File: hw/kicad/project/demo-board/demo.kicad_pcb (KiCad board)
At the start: 2 copper layers, 49.5 x 49.5 mm, 20 parts, among them P1 CONN_01X16, P2 CONN_01X16, SW1 KEY_FLASH, SW2 KEY_RST, U1 NCP1117ST33T3G, U2 ESP-12E

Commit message: Freeroute applied
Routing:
- net /SPI_INT: track 0.00 -> 46.5 mm
- net /TXD0: track 0.00 -> 46.1 mm
- net /RXD0: track 0.00 -> 45.7 mm
- net /GPIO10: track 0.00 -> 43.4 mm, vias 0 -> 1
- net /GPIO0: track 0.00 -> 40.2 mm, vias 0 -> 1
- net /nRST: track 42.1 -> 80.1 mm
- net Net-(JP1-Pad2): track 0.00 -> 33.5 mm
- net /GPIO13: track 0.00 -> 32.3 mm
- net /GPIO12: track 0.00 -> 32.1 mm
- net /GPIO14: track 0.00 -> 31.9 mm
- net /EN: track 12.6 -> 42.5 mm
- net /GPIO16: track 10.2 -> 38.9 mm
- net VCC: track 60.6 -> 89.0 mm, vias 2 -> 3
- net /SPI_CLK: track 0.00 -> 28.2 mm
- net /GPIO9: track 0.00 -> 26.7 mm
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
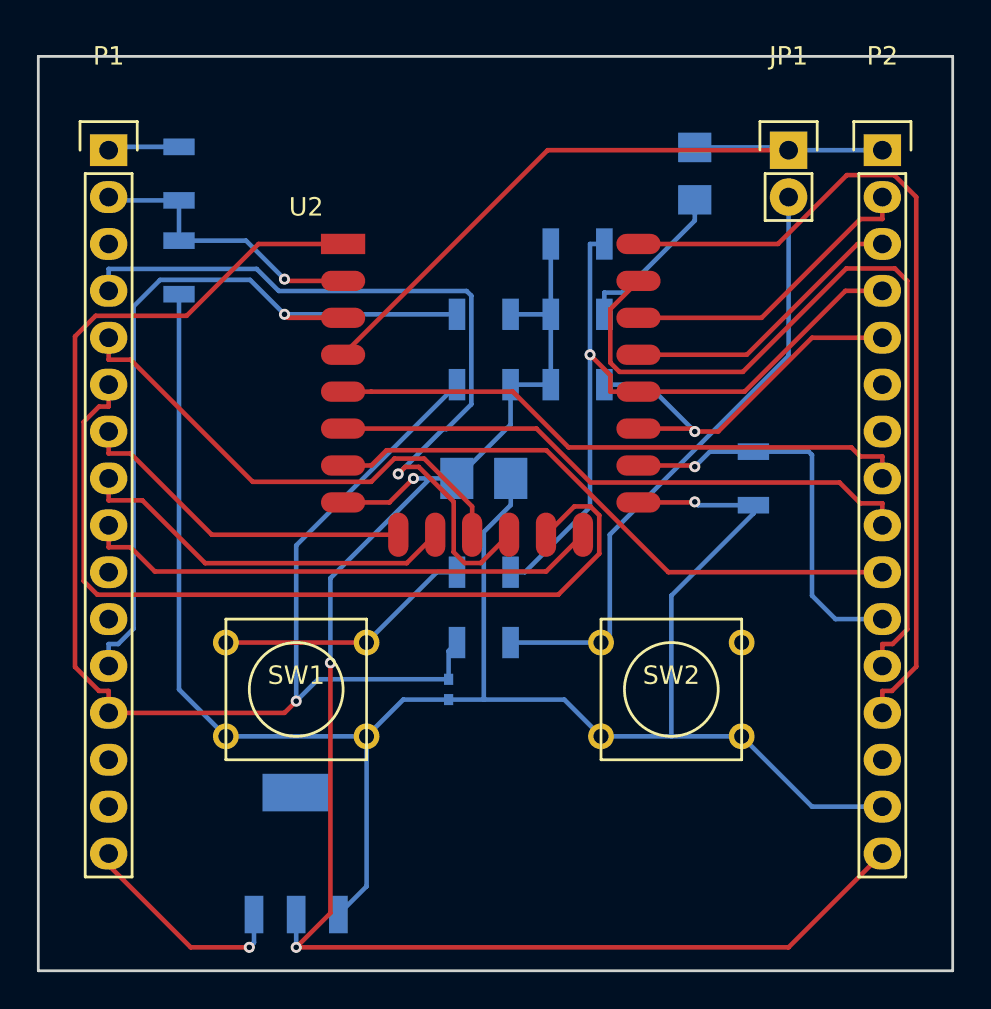
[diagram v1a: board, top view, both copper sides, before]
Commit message: Ited studio requirements added
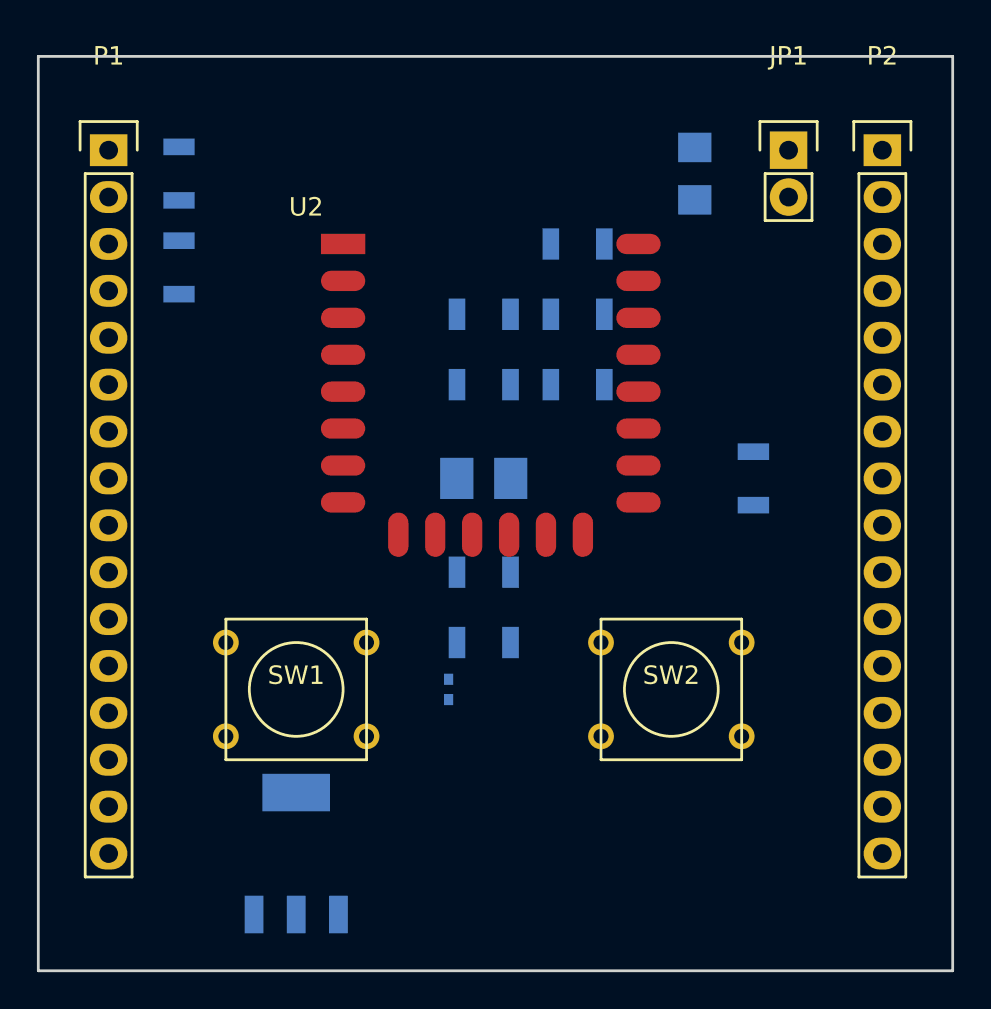
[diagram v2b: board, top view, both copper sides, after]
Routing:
- net GND: track 107.5 -> 0.00 mm, vias 1 -> 0
- net VCC: track 89.0 -> 0.00 mm, vias 3 -> 0
- net /nRST: track 80.1 -> 0.00 mm, vias 1 -> 0
- net /SPI_INT: track 46.5 -> 0.00 mm
- net /TXD0: track 46.1 -> 0.00 mm
- net /RXD0: track 45.7 -> 0.00 mm
- net /GPIO10: track 43.4 -> 0.00 mm, vias 1 -> 0
- net /EN: track 42.5 -> 0.00 mm, vias 1 -> 0
- net /GPIO0: track 40.2 -> 0.00 mm, vias 1 -> 0
- net /GPIO16: track 38.9 -> 0.00 mm
- net Net-(JP1-Pad2): track 33.5 -> 0.00 mm
- net /GPIO13: track 32.3 -> 0.00 mm
- net /GPIO12: track 32.1 -> 0.00 mm
- net /GPIO14: track 31.9 -> 0.00 mm
- net /SPI_CLK: track 28.2 -> 0.00 mm
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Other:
- net class Default: clearance 0.2 -> 0.2032; trace_width 0.25 -> 0.2032; via_dia 0.6 -> 0.61; via_drill 0.4 -> 0.41
- net class Itead signal added: clearance 0.2032, trace_width 0.2032, via_dia 0.61, via_drill 0.41
- rule pad_to_mask_clearance: 0.2 -> -0.12
- rule trace_clearance: 0.2 -> 0.2032
- rule trace_min: 0.2 -> 0.2032
- rule via_min_drill: 0.3 -> 0.41
- rule via_min_size: 0.4 -> 0.61

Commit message: Added SD card and 3d shapes
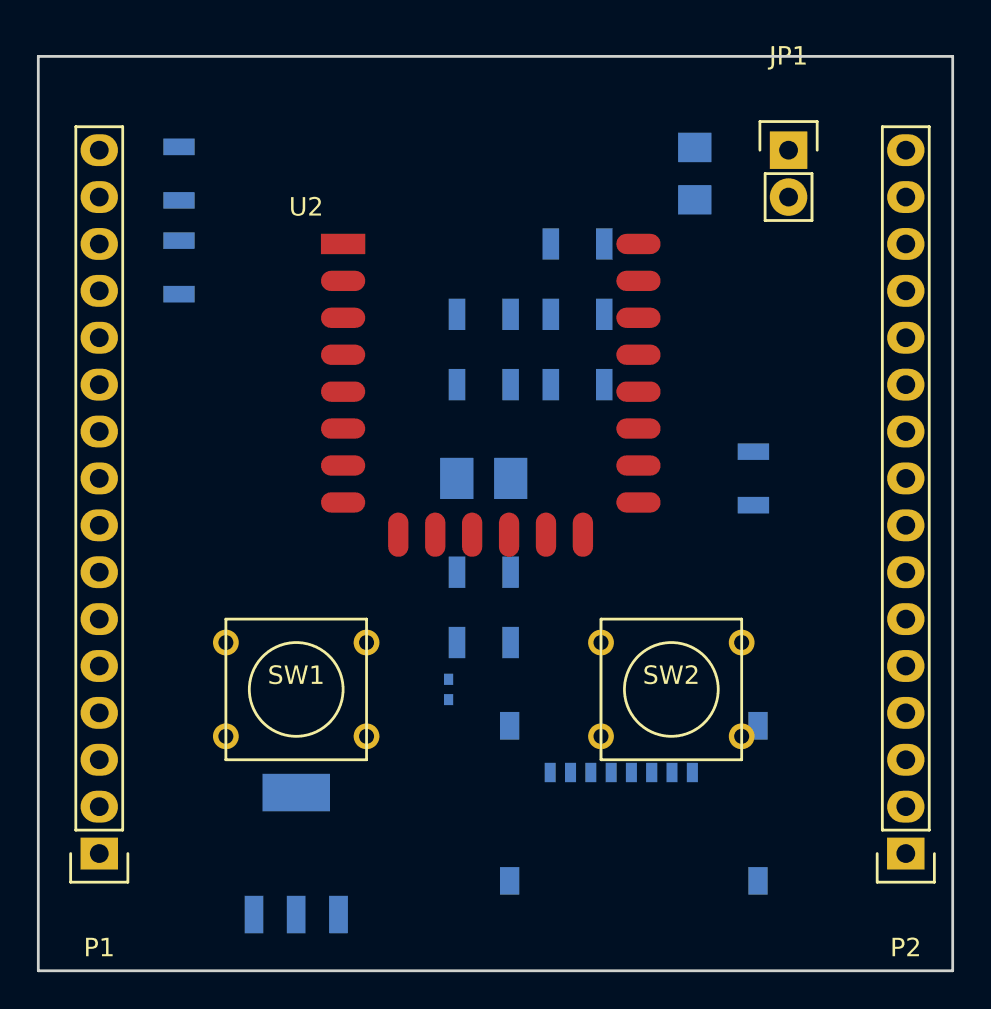
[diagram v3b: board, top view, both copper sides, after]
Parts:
- added J1: MicroSD, armory:MICRO_SD_HINGE_AMP, B.Cu at (155.4, 118.1)
- U2: footprint ESP8266:ESP-12E -> ESP8266:ESP-12E_with_3d
- moved P2 38.1 mm to (170.2, 113.0), turned to 180 degrees
- moved P1 38.1 mm to (126.5, 113.0), turned to 180 degrees

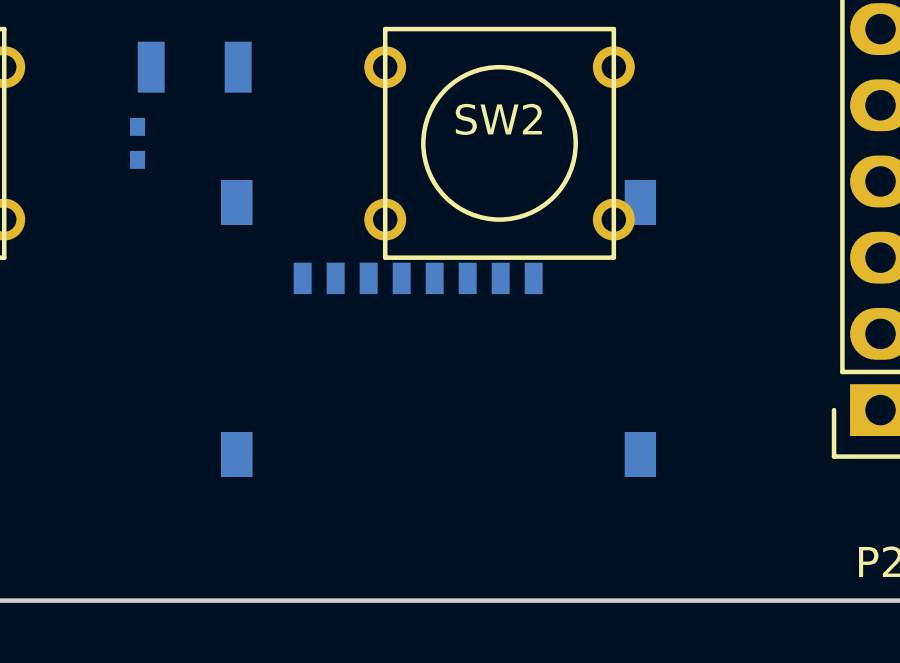
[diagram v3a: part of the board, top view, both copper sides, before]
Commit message: Improve library management
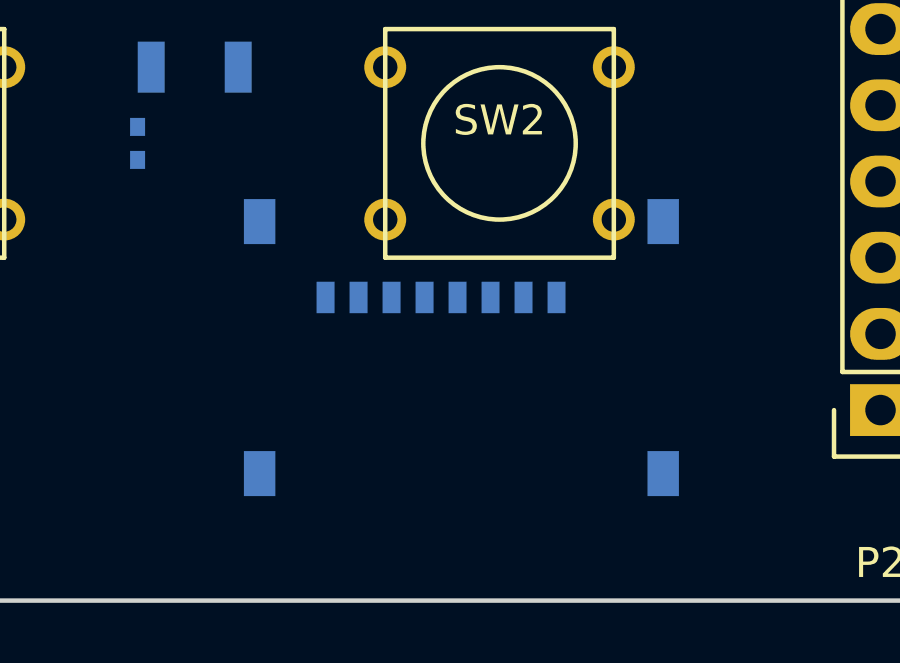
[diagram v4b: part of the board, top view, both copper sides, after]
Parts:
- removed J1: MicroSD, armory:MICRO_SD_HINGE_AMP
- added J2: MICRO_SD_HINGE, armory_local:MICRO_SD_HINGE_AMP, B.Cu at (156.2, 118.7)
- U2: footprint ESP8266:ESP-12E_with_3d -> ESP8266_local:ESP-12E_with_3d
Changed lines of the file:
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@@
     (zones 0)
     (modules 21)
-    (nets 44)
+    (nets 48)
   )
   (page A4)
@@
   (net 34 "Net-(P2-Pad14)")
   (net 35 "Net-(R1-Pad2)")
-  (net 36 "Net-(J1-Pad1)")
-  (net 37 "Net-(J1-Pad2)")
-  (net 38 "Net-(J1-Pad3)")
-  (net 39 "Net-(J1-Pad4)")
-  (net 40 "Net-(J1-Pad5)")
-  (net 41 "Net-(J1-Pad6)")
-  (net 42 "Net-(J1-Pad7)")
-  (net 43 "Net-(J1-Pad8)")
+  (net 36 "Net-(J2-Pad1)")
+  (net 37 "Net-(J2-Pad2)")
+  (net 38 "Net-(J2-Pad3)")
+  (net 39 "Net-(J2-Pad4)")
+  (net 40 "Net-(J2-Pad5)")
+  (net 41 "Net-(J2-Pad6)")
+  (net 42 "Net-(J2-Pad7)")
+  (net 43 "Net-(J2-Pad8)")
+  (net 44 "Net-(J2-Pad12)")
+  (net 45 "Net-(J2-Pad9)")
+  (net 46 "Net-(J2-Pad11)")
+  (net 47 "Net-(J2-Pad10)")
   (net_class Default "This is the default net class."
     (clearance 0.2032)
@@
     (add_net GND)
     (add_net "Net-(D1-Pad2)")
-    (add_net "Net-(J1-Pad1)")
-    (add_net "Net-(J1-Pad2)")
-    (add_net "Net-(J1-Pad3)")
-    (add_net "Net-(J1-Pad4)")
-    (add_net "Net-(J1-Pad5)")
-    (add_net "Net-(J1-Pad6)")
-    (add_net "Net-(J1-Pad7)")
-    (add_net "Net-(J1-Pad8)")
+    (add_net "Net-(J2-Pad1)")
+    (add_net "Net-(J2-Pad10)")
+    (add_net "Net-(J2-Pad11)")
+    (add_net "Net-(J2-Pad12)")
+    (add_net "Net-(J2-Pad2)")
+    (add_net "Net-(J2-Pad3)")
+    (add_net "Net-(J2-Pad4)")
+    (add_net "Net-(J2-Pad5)")
+    (add_net "Net-(J2-Pad6)")
+    (add_net "Net-(J2-Pad7)")
+    (add_net "Net-(J2-Pad8)")
+    (add_net "Net-(J2-Pad9)")
     (add_net "Net-(JP1-Pad2)")
     (add_net "Net-(P1-Pad10)")
@@
       (net 1 GND))
   )
-  (module armory:MICRO_SD_HINGE_AMP (layer B.Cu)
-    (at 155.448 118.11)
-    (attr smd)
-    (fp_text reference J1 (at 0.01524 -6.20268) (layer B.SilkS)
-      (effects (font (thickness 0.3048)) (justify mirror))
-    )
-    (fp_text value MicroSD (at -0.01524 -8.01116) (layer B.SilkS) hide
-      (effects (font (size 1 1) (thickness 0.25)) (justify mirror))
-    )
-    (fp_line (start 6.79958 0) (end 6.79958 -13.29944) (layer B.SilkS) (width 0.20066))
-    (fp_line (start 6.79958 -13.29944) (end -6.79958 -13.29944) (layer B.SilkS) (width 0.20066))
-    (fp_line (start -6.79958 -13.29944) (end -6.79958 0) (layer B.SilkS) (width 0.20066))
-    (fp_line (start -6.79958 0) (end 6.79958 0) (layer B.SilkS) (width 0.20066))
-    (pad 1 smd rect (at 3.16992 -9.46912) (size 0.59944 1.04902) (layers B.Cu B.Paste B.Mask)
-      (net 36 "Net-(J1-Pad1)"))
-    (pad 2 smd rect (at 2.0701 -9.46912) (size 0.59944 1.04902) (layers B.Cu B.Paste B.Mask)
-      (net 37 "Net-(J1-Pad2)"))
-    (pad 3 smd rect (at 0.97028 -9.46912) (size 0.59944 1.04902) (layers B.Cu B.Paste B.Mask)
-      (net 38 "Net-(J1-Pad3)"))
-    (pad 4 smd rect (at -0.12954 -9.46912) (size 0.59944 1.04902) (layers B.Cu B.Paste B.Mask)
-      (net 39 "Net-(J1-Pad4)"))
-    (pad 5 smd rect (at -1.22936 -9.46912) (size 0.59944 1.04902) (layers B.Cu B.Paste B.Mask)
-      (net 40 "Net-(J1-Pad5)"))
-    (pad 6 smd rect (at -2.32918 -9.46912) (size 0.59944 1.04902) (layers B.Cu B.Paste B.Mask)
-      (net 41 "Net-(J1-Pad6)"))
-    (pad 7 smd rect (at -3.429 -9.46912) (size 0.59944 1.04902) (layers B.Cu B.Paste B.Mask)
-      (net 42 "Net-(J1-Pad7)"))
-    (pad 8 smd rect (at -4.52882 -9.46912) (size 0.59944 1.04902) (layers B.Cu B.Paste B.Mask)
-      (net 43 "Net-(J1-Pad8)"))
-    (pad 12 smd rect (at 6.72592 -11.99896) (size 1.04902 1.50114) (layers B.Cu B.Paste B.Mask))
-    (pad 9 smd rect (at -6.72592 -11.99896) (size 1.04902 1.50114) (layers B.Cu B.Paste B.Mask))
-    (pad 11 smd rect (at 6.72592 -3.59918) (size 1.04902 1.50114) (layers B.Cu B.Paste B.Mask))
-    (pad 10 smd rect (at -6.72592 -3.59918) (size 1.04902 1.50114) (layers B.Cu B.Paste B.Mask))
-    (model 3D/SD-Amp-microSlot.wrl
-      (at (xyz 0 -0.261181 0))
-      (scale (xyz 0.3937 0.3937 0.3937))
-      (rotate (xyz 0 0 0))
-    )
-  )
-  (module ESP8266:ESP-12E_with_3d (layer F.Cu)
+  (module ESP8266_local:ESP-12E_with_3d (layer F.Cu)
     (at 139.7 80.01)
     (descr "Module, ESP-8266, ESP-12, 16 pad, SMD")
@@
     (pad 22 smd oval (at 16 0) (size 2.4 1.1) (layers F.Cu F.Paste F.Mask)
       (net 33 /TXD0))
-    (model ${HOME}/kicad_ecf_project/hw/kicad/libs/3rd-party/kicad-ESP8266/ESP8266.3dshapes/ESP-12.wrl
+    (model ${HOME}/kicad_ecf_project/hw/kicad/libs/self/kicad-ESP8266_local/ESP8266.3dshapes/ESP-12.wrl
       (at (xyz 0.048 0 0))
       (scale (xyz 0.39 0.39 0.39))
       (rotate (xyz 0 0 0))
     )
+  )
+  (module armory_local:MICRO_SD_HINGE_AMP (layer B.Cu)
+    (at 156.21 118.745)
+    (attr smd)
+    (fp_text reference J2 (at 0.01524 -6.20268) (layer B.SilkS)
+      (effects (font (thickness 0.3048)) (justify mirror))
+    )
+    (fp_text value MICRO_SD_HINGE (at -0.01524 -8.01116) (layer B.SilkS) hide
+      (effects (font (size 1 1) (thickness 0.25)) (justify mirror))
+    )
+    (fp_line (start 6.79958 0) (end 6.79958 -13.29944) (layer B.SilkS) (width 0.20066))
+    (fp_line (start 6.79958 -13.29944) (end -6.79958 -13.29944) (layer B.SilkS) (width 0.20066))
+    (fp_line (start -6.79958 -13.29944) (end -6.79958 0) (layer B.SilkS) (width 0.20066))
+    (fp_line (start -6.79958 0) (end 6.79958 0) (layer B.SilkS) (width 0.20066))
+    (pad 1 smd rect (at 3.16992 -9.46912) (size 0.59944 1.04902) (layers B.Cu B.Paste B.Mask)
+      (net 36 "Net-(J2-Pad1)"))
+    (pad 2 smd rect (at 2.0701 -9.46912) (size 0.59944 1.04902) (layers B.Cu B.Paste B.Mask)
+      (net 37 "Net-(J2-Pad2)"))
+    (pad 3 smd rect (at 0.97028 -9.46912) (size 0.59944 1.04902) (layers B.Cu B.Paste B.Mask)
+      (net 38 "Net-(J2-Pad3)"))
+    (pad 4 smd rect (at -0.12954 -9.46912) (size 0.59944 1.04902) (layers B.Cu B.Paste B.Mask)
+      (net 39 "Net-(J2-Pad4)"))
+    (pad 5 smd rect (at -1.22936 -9.46912) (size 0.59944 1.04902) (layers B.Cu B.Paste B.Mask)
+      (net 40 "Net-(J2-Pad5)"))
+    (pad 6 smd rect (at -2.32918 -9.46912) (size 0.59944 1.04902) (layers B.Cu B.Paste B.Mask)
+      (net 41 "Net-(J2-Pad6)"))
+    (pad 7 smd rect (at -3.429 -9.46912) (size 0.59944 1.04902) (layers B.Cu B.Paste B.Mask)
+      (net 42 "Net-(J2-Pad7)"))
+    (pad 8 smd rect (at -4.52882 -9.46912) (size 0.59944 1.04902) (layers B.Cu B.Paste B.Mask)
+      (net 43 "Net-(J2-Pad8)"))
+    (pad 12 smd rect (at 6.72592 -11.99896) (size 1.04902 1.50114) (layers B.Cu B.Paste B.Mask)
+      (net 44 "Net-(J2-Pad12)"))
+    (pad 9 smd rect (at -6.72592 -11.99896) (size 1.04902 1.50114) (layers B.Cu B.Paste B.Mask)
+      (net 45 "Net-(J2-Pad9)"))
+    (pad 11 smd rect (at 6.72592 -3.59918) (size 1.04902 1.50114) (layers B.Cu B.Paste B.Mask)
+      (net 46 "Net-(J2-Pad11)"))
+    (pad 10 smd rect (at -6.72592 -3.59918) (size 1.04902 1.50114) (layers B.Cu B.Paste B.Mask)
+      (net 47 "Net-(J2-Pad10)"))
+    (model ${HOME}/kicad_ecf_project/hw/kicad/libs/self/usbarmory_local/3D/SD-Amp-microSlot.wrl
+      (at (xyz 0 -0.26 0))
+      (scale (xyz 0.3777 0.3777 0.3777))
+      (rotate (xyz 0 0 0))
+    )

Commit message: Board routes part 1
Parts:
- removed D1: LED, LEDs:LED-1206
- removed R4, R5: 470, Resistors_SMD:R_1206
- added C3: 1nF, Capacitors_SMD:C_0402, B.Cu at (149.9, 102.9)
- added P3: ESP_CONN, Pin_Headers:Pin_Header_Straight_1x07, F.Cu at (161.3, 104.1)
- added P4: PWR_CONN, Pin_Headers:Pin_Header_Straight_1x03, F.Cu at (163.8, 74.9)
- added P5: CONN_DISPLAY, display_local:Nokia_5110_LCD, B.Cu at (141.0, 116.8)
- added P6: SD_LCD_CONN, Pin_Headers:Pin_Header_Straight_1x07, F.Cu at (141.0, 72.4)
- added R11: 50k, Resistors_SMD:R_1206, B.Cu at (146.1, 94.0)
- added R12: 50k, Resistors_SMD:R_1206, B.Cu at (128.3, 99.1)
- added R13: 50k, Resistors_SMD:R_1206, B.Cu at (128.3, 104.1)
- added R14: 50k, Resistors_SMD:R_1206, B.Cu at (128.3, 101.6)
- added R15: 50k, Resistors_SMD:R_1206, B.Cu at (128.3, 96.5)
- P1, P2: value CONN_01X16 -> ESP_CONN; footprint Pin_Headers:Pin_Header_Straight_1x16 -> Pin_Headers:Pin_Header_Straight_1x07
- moved J2 55.1 mm to (130.8, 69.8), turned to 180 degrees
- moved U1 41.3 mm to (165.1, 82.5), turned to 270 degrees
- moved JP1 35.9 mm to (130.8, 88.9), turned to 270 degrees
- moved R2 33.1 mm to (128.3, 109.2), turned to 0 degrees
- moved SW1 33.0 mm to (168.9, 113.0), turned to 270 degrees
- moved P2 30.3 mm to (140.0, 110.5), turned to 90 degrees
- moved SW2 30.2 mm to (129.5, 115.6)
- moved P1 25.9 mm to (135.9, 88.9), turned to 0 degrees
- moved R3 25.5 mm to (128.3, 106.7), turned to 180 degrees
- moved R8 22.3 mm to (132.1, 100.1), turned to 90 degrees
- moved R10 21.6 mm to (162.6, 114.3)
- moved R6 15.5 mm to (149.9, 95.2)
- moved R7 15.3 mm to (153.7, 102.9)
- moved C2 14.0 mm to (144.8, 90.2), turned to 0 degrees
- moved U2 10.2 mm to (141.0, 90.2)
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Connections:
- J2 pad 10: Net-(J2-Pad10) -> GND
- J2 pad 11: Net-(J2-Pad11) -> GND
- J2 pad 12: Net-(J2-Pad12) -> GND
- J2 pad 2: Net-(J2-Pad2) -> /SD_CS
- J2 pad 3: Net-(J2-Pad3) -> /SD_LCD_MOSI
- J2 pad 4: Net-(J2-Pad4) -> VCC
- J2 pad 5: Net-(J2-Pad5) -> /SD_LCD_CLK
- J2 pad 6: Net-(J2-Pad6) -> GND
- J2 pad 7: Net-(J2-Pad7) -> /SD_LCD_MISO
- J2 pad 9: Net-(J2-Pad9) -> GND
- JP1 pad 1: /GPIO16 -> /nRST
- P1 pad 1: /ADC_EX -> /nRST
- P1 pad 3: Net-(P1-Pad3) -> /EN
- P1 pad 4: /GPIO10 -> /GPIO16
- P1 pad 5: /GPIO9 -> /GPIO14
- P1 pad 6: /SPI_INT -> /GPIO12
- P1 pad 7: /SPI_MOSI -> /GPIO13
- P2 pad 1: /GPIO16 -> /ADC_EX
- P2 pad 2: /GPIO5 -> /SPI_MOSI
- P2 pad 3: /GPIO4 -> /SPI_MISO
- P2 pad 4: /GPIO0 -> /GPIO9
- P2 pad 5: /GPIO2 -> /GPIO10
- P2 pad 6: Net-(P2-Pad6) -> /SPI_INT
- P2 pad 7: Net-(P2-Pad7) -> /SPI_CLK
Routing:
- net VCC: track 0.00 -> 128.4 mm, vias 0 -> 1
- net GND: track 0.00 -> 76.1 mm, vias 0 -> 2
- net /LCD_RST: track 0.00 -> 73.1 mm, vias 0 -> 1
- net /LCD_CS: track 0.00 -> 67.1 mm, vias 0 -> 1
- net /SD_LCD_DATA_CMD: track 0.00 -> 64.5 mm, vias 0 -> 1
- net Net-(R1-Pad2): track 0.00 -> 48.1 mm
- net Net-(JP1-Pad2): track 0.00 -> 32.8 mm
- net /nRST: track 0.00 -> 27.4 mm, vias 0 -> 1
- net /GPIO15: track 0.00 -> 14.4 mm
- net /GPIO2: track 0.00 -> 13.1 mm, vias 0 -> 1
- net /EN: track 0.00 -> 12.7 mm
- net /GPIO0: track 0.00 -> 12.3 mm, vias 0 -> 1
- net 5V: track 0.00 -> 11.3 mm
- net /ADC_EX: track 0.00 -> 10.8 mm, vias 0 -> 1
- net /ADC: track 0.00 -> 7.92 mm
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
